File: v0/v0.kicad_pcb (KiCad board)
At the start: 2 copper layers, 101.5 x 83 mm, 35 parts, among them CON1 SNES-CONN, U1 SN74LV165APWR, U2 SN74LV165APWR, U3 SN74LV165APWR, U4 SN74LVC8T245PWR, U5 PIC12F629-ISN, U6 AMS1117-3.3

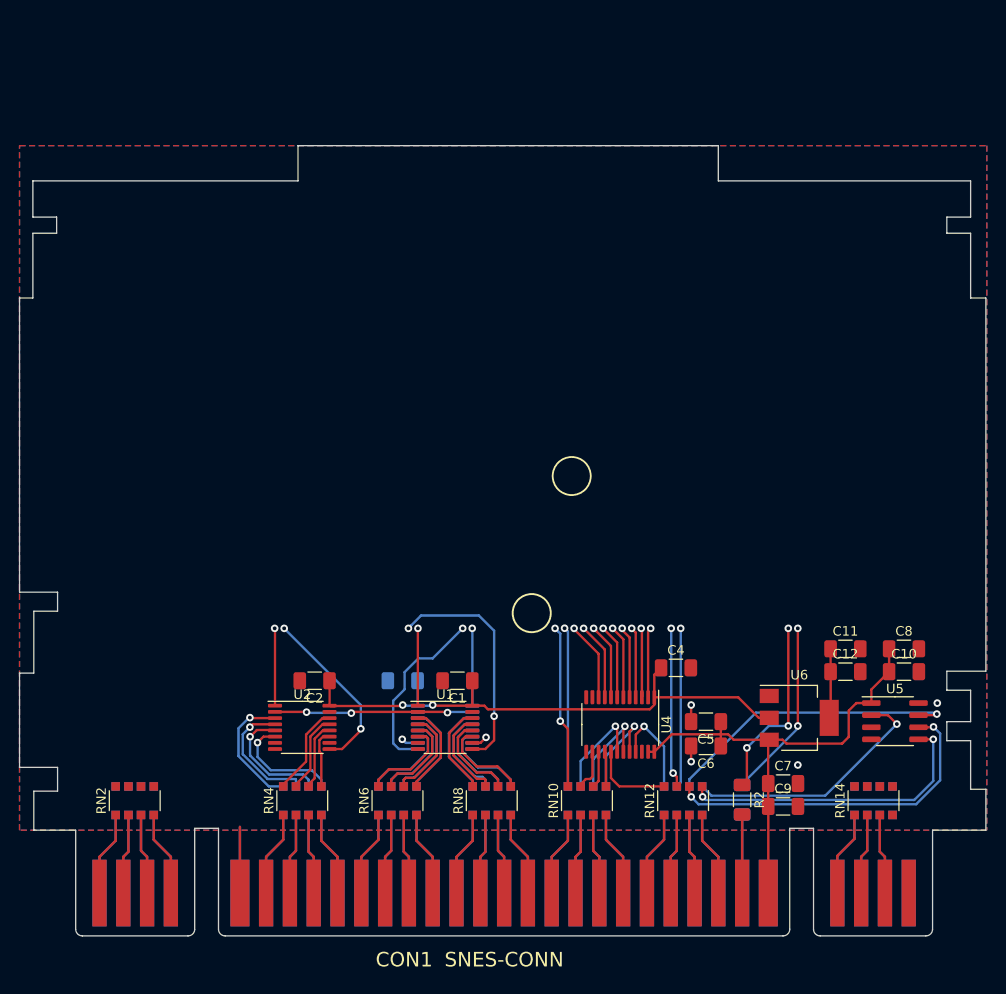
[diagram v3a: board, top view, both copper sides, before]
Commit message: Added RPi Pico footprint and routed traces to it
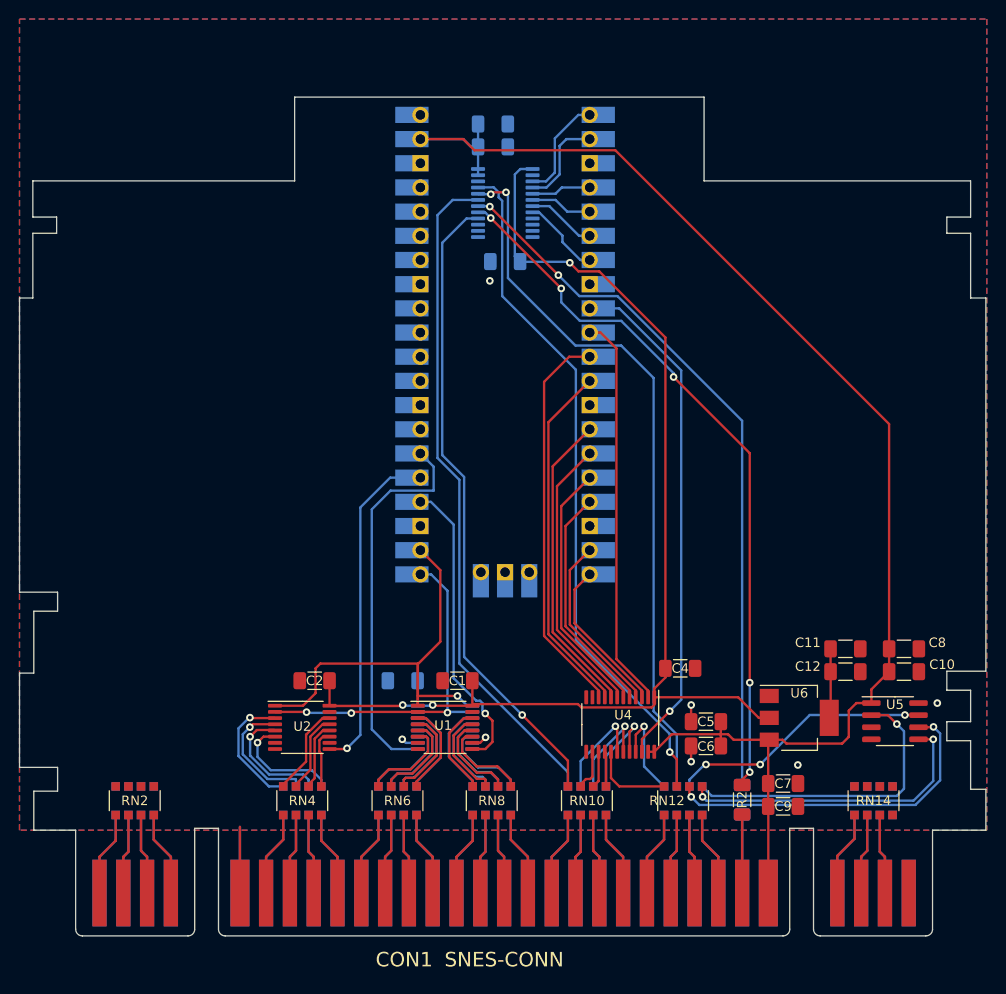
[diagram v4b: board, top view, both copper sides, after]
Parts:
- added C13: 0.1uF, Capacitor_SMD:C_1206_3216Metric_Pad1.33x1.80mm_HandSolder, B.Cu at (137.3, 63.0)
- added C14: 0.1uF, Capacitor_SMD:C_1206_3216Metric_Pad1.33x1.80mm_HandSolder, B.Cu at (136.0, 50.9)
- added C15: 1uF, Capacitor_SMD:C_1206_3216Metric_Pad1.33x1.80mm_HandSolder, B.Cu at (136.0, 48.5)
- added U7: SN74LVC8T245PWR, Package_SO:TSSOP-24_4.4x7.8mm_P0.65mm, B.Cu at (137.3, 56.8)
- added U8: Pico, RP-Pico:RPi_Pico_SMD_TH, B.Cu at (137.3, 71.7)
- moved C4 0.45 mm to (155.7, 105.7)
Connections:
- RN13 pad 5: unconnected-(RN13-Pad5) -> /YPA1
- RN13 pad 6: unconnected-(RN13-Pad6) -> /YPA3
- RN13 pad 7: unconnected-(RN13-Pad7) -> /YPA5
- U2 pad 1: /U2~{LD} -> /U1~{LD}
- U3 pad 1: /U3~{LD} -> /U1~{LD}
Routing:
- net +5V: track 53.2 -> 150.0 mm
- net +3.3V: track 66.9 -> 131.5 mm, vias 2 -> 3
- net /Y~{WR}: track 16.8 -> 75.7 mm, vias 1 -> 2
- net /YCPU_CLK: track 18.9 -> 75.3 mm
- net /Y~{RESET}: track 19.7 -> 76.0 mm, vias 3 -> 5
- net /Y~{RD}: track 16.8 -> 72.5 mm, vias 2 -> 1
- net /Y~{CE}: track 16.8 -> 70.6 mm, vias 1 -> 0
- net /D~{OE}: track 0.00 -> 52.5 mm, vias 0 -> 1
- net /Y~{IRQ}: track 17.2 -> 67.4 mm, vias 2 -> 1
- net /U1~{LD}: track 8.13 -> 46.6 mm
- net /DDIR: track 7.35 -> 41.5 mm, vias 1 -> 0
- net /D0: track 8.30 -> 41.4 mm, vias 1 -> 0
- net /D1: track 8.16 -> 37.5 mm, vias 1 -> 0
- net /D2: track 7.99 -> 32.3 mm, vias 1 -> 0
- net /D3: track 7.85 -> 29.7 mm, vias 1 -> 0
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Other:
- board size 101.5 x 83 mm -> 101.5 x 88.1 mm

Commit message: Connect /OE to GND; fix up minor routing
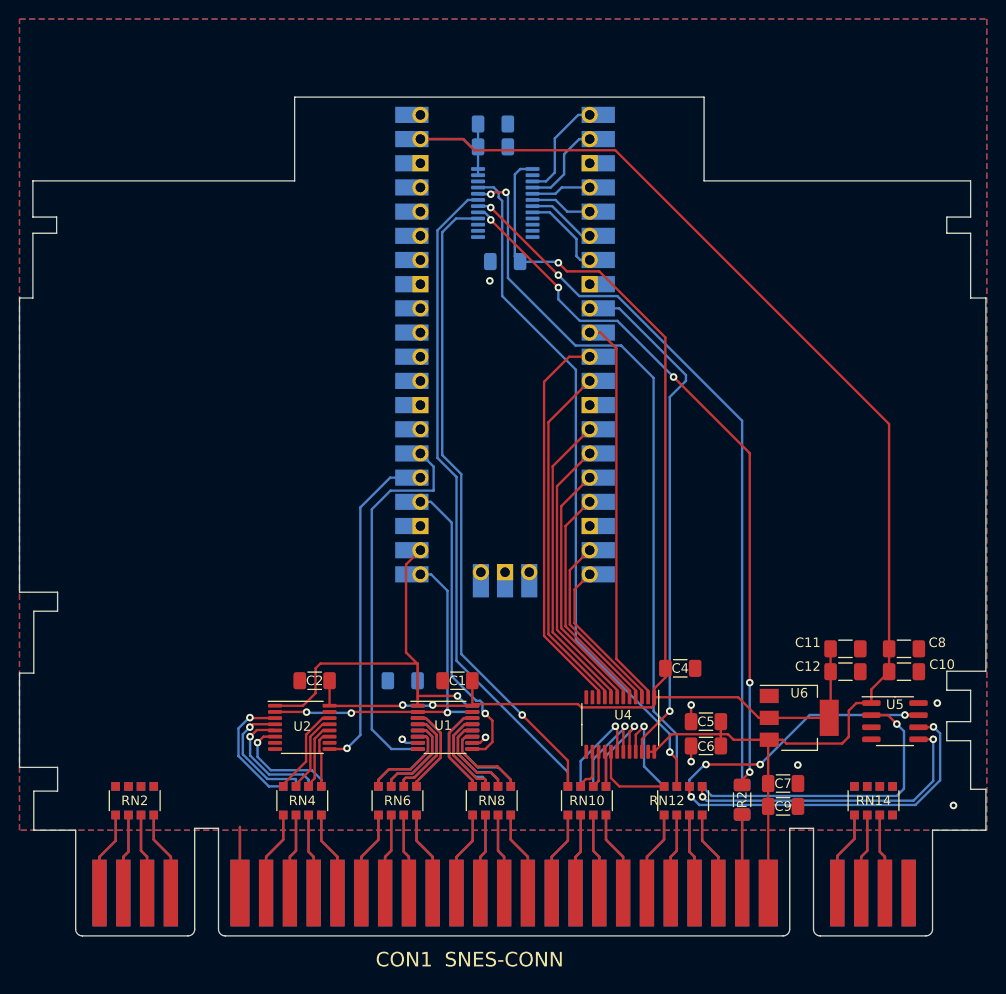
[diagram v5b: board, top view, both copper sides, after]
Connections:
- U7 pad 10: GND -> /U7A8
- U7 pad 14: GND -> /U7B8
- U7 pad 15: GND -> /U7B7
- U7 pad 22: unconnected-(U7-Pad22) -> GND
- U7 pad 9: GND -> /U7A7
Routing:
- net +3.3V: track 131.5 -> 137.8 mm
- net /Y~{RESET}: track 76.0 -> 75.0 mm
- net /Y~{CE}: track 70.6 -> 69.7 mm
- net /U1~{LD}: track 46.6 -> 45.9 mm
- net /~{IRQ}: track 8.47 -> 9.13 mm
- net /Y~{IRQ}: track 67.4 -> 68.0 mm
- net /~{WR}: track 9.87 -> 9.34 mm
- net GND: vias 7 -> 8

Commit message: Added front and back indicators; added title
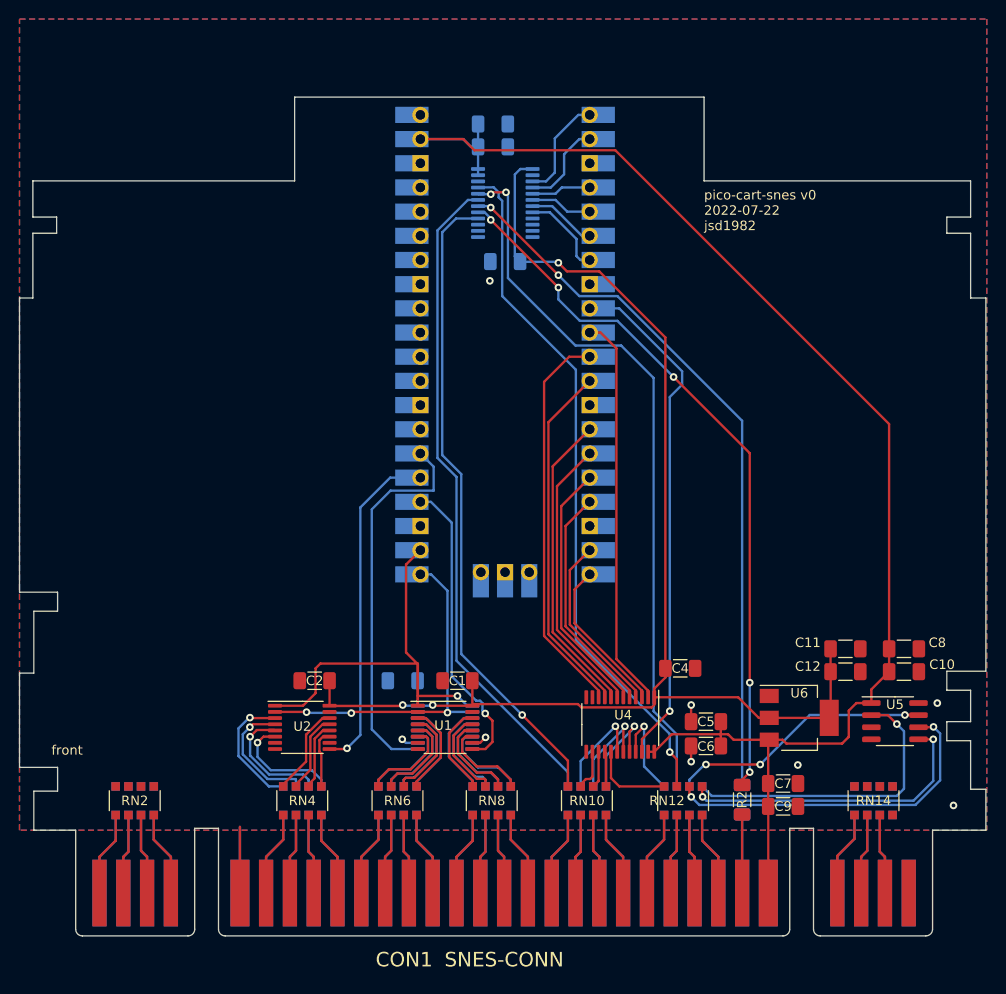
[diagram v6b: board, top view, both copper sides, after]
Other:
- board text added: "back"
- board text added: "front"
- board text added: "pico-cart-snes v0 2022-07-22 jsd1982"
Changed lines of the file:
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@@
     (property "Sheetname" "")
     (attr smd)
-    (fp_text reference "R1" (at 0 1.82 90) (layer "B.SilkS")
+    (fp_text reference "R1" (at 0 0.1 90) (layer "B.SilkS")
       (effects (font (size 1 1) (thickness 0.15)) (justify mirror))
     )
@@
       (rotate (xyz 0 0 0))
     )
+  )
+  (gr_text "back" (at 91.2 114.3) (layer "B.SilkS")
+    (effects (font (size 1 1) (thickness 0.15)) (justify mirror))
+  )
+  (gr_text "pico-cart-snes v0\n2022-07-22\njsd1982" (at 158.2 57.6) (layer "F.SilkS")
+    (effects (font (size 1 1) (thickness 0.15)) (justify left))
+  )
+  (gr_text "front" (at 91.3 114.3) (layer "F.SilkS")
+    (effects (font (size 1 1) (thickness 0.15)))
   )
   (segment (start 94.70072 125.49928) (end 96.4 123.8) (width 0.25) (layer "F.Cu") (net 1))
@@
   (segment (start 151.675 113.125) (end 154.599998 110.2) (width 0.25) (layer "F.Cu") (net 139))
   (via (at 154.599998 110.2) (size 0.8) (drill 0.4) (layers "F.Cu" "B.Cu") (net 139))
-  (segment (start 149.29 67.89) (end 156.3 74.9) (width 0.25) (layer "B.Cu") (net 139))
+  (segment (start 154.599998 77.200002) (end 154.599998 110.2) (width 0.25) (layer "B.Cu") (net 139))
+  (segment (start 155.9 75.9) (end 154.599998 77.200002) (width 0.25) (layer "B.Cu") (net 139))
+  (segment (start 155.9 74.5) (end 155.9 75.9) (width 0.25) (layer "B.Cu") (net 139))
+  (segment (start 149.29 67.89) (end 155.9 74.5) (width 0.25) (layer "B.Cu") (net 139))
   (segment (start 147.8 67.89) (end 149.29 67.89) (width 0.25) (layer "B.Cu") (net 139))
-  (segment (start 156.3 74.9) (end 156.3 75.5) (width 0.25) (layer "B.Cu") (net 139))
-  (segment (start 154.599998 77.200002) (end 154.599998 110.2) (width 0.25) (layer "B.Cu") (net 139))
-  (segment (start 156.3 75.5) (end 154.599998 77.200002) (width 0.25) (layer "B.Cu") (net 139))
   (segment (start 140.1875 57.8) (end 142 57.8) (width 0.25) (layer "B.Cu") (net 142))
   (segment (start 144.8 60.6) (end 144.8 62.4) (width 0.25) (layer "B.Cu") (net 142))

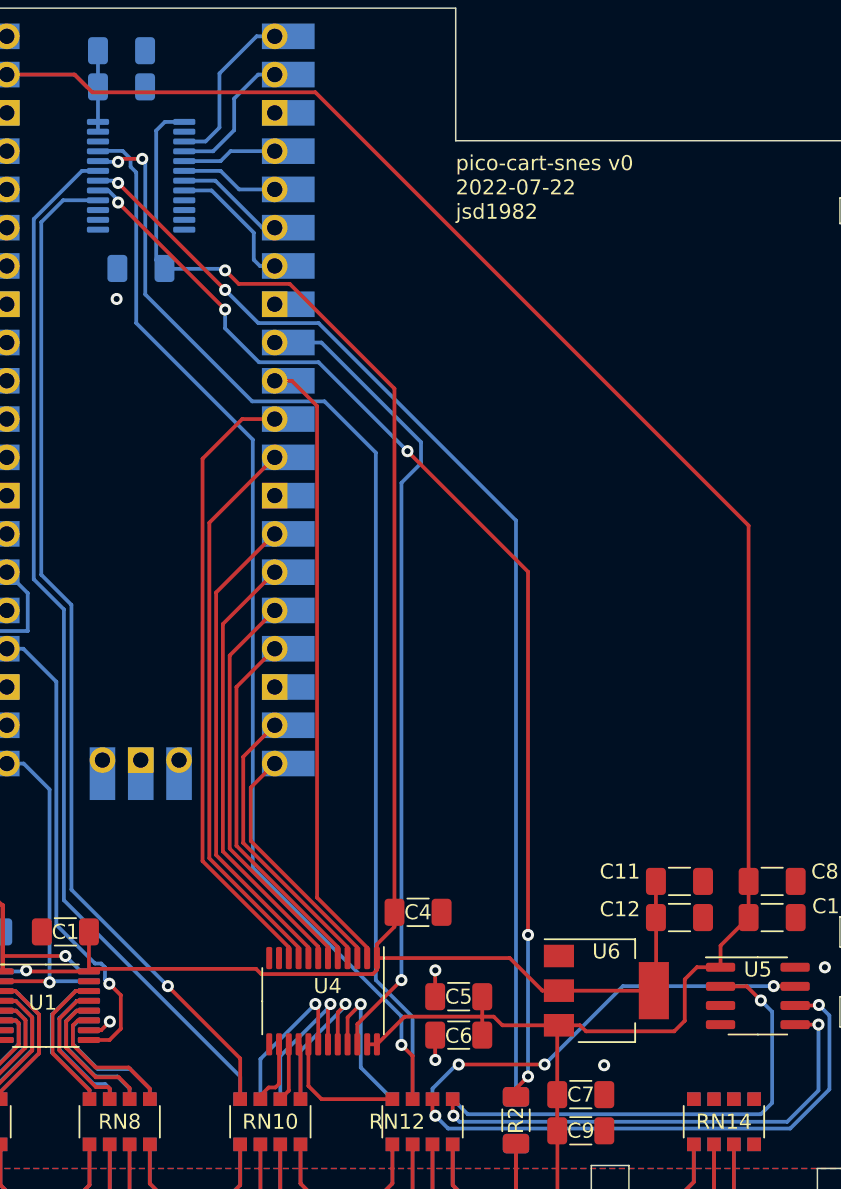
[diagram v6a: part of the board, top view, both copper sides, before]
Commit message: Add title to back layer; render front/back PCB and schematic
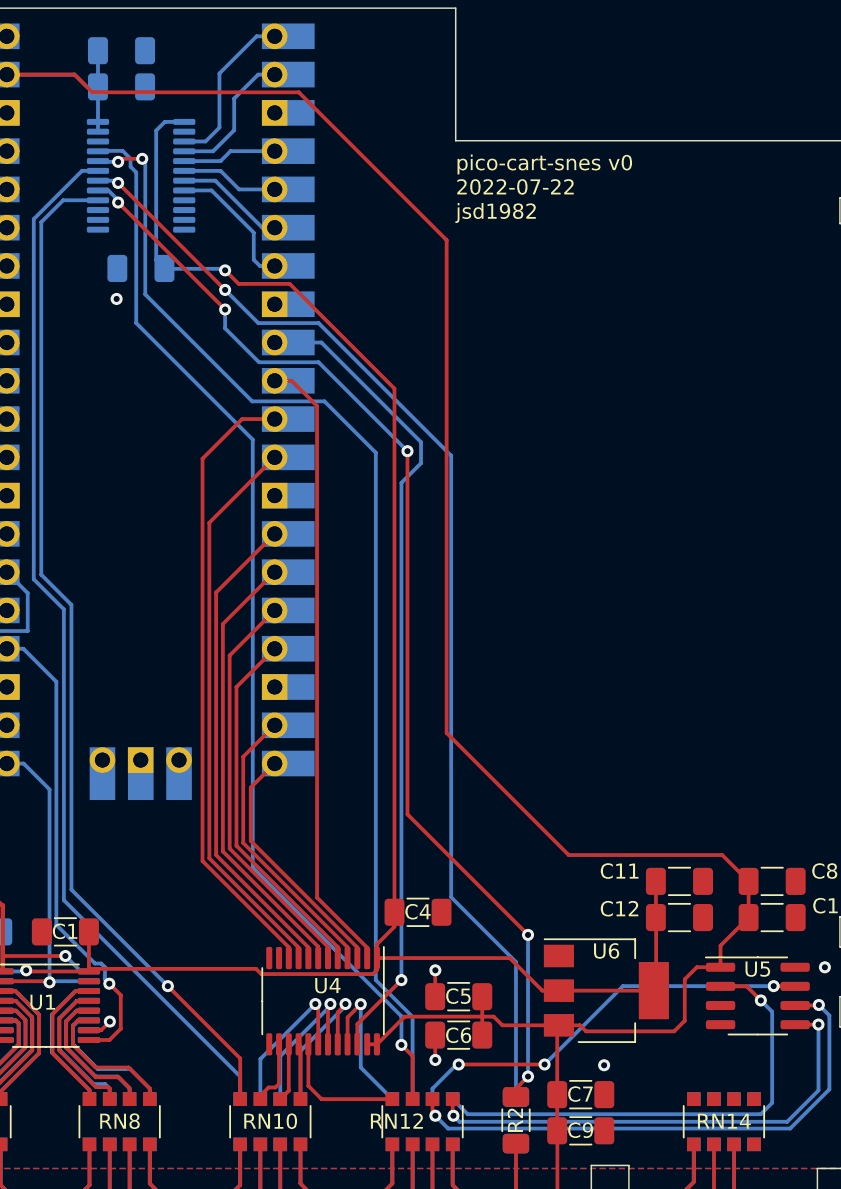
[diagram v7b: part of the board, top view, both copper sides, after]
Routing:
- net +5V: track 150.0 -> 155.3 mm
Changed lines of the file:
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@@
     )
+  )
+  (gr_text "pico-cart-snes v0\n2022-07-22\njsd1982" (at 172.8 57.6) (layer "B.SilkS")
+    (effects (font (size 1 1) (thickness 0.15)) (justify left mirror))
   )
   (gr_text "back" (at 91.2 114.3) (layer "B.SilkS")
@@
   (segment (start 162.20122 129.30038) (end 162.20122 121.05122) (width 0.25) (layer "F.Cu") (net 26))
   (segment (start 172.7 113.6) (end 173.4 112.9) (width 0.25) (layer "F.Cu") (net 27))
-  (segment (start 148.885 51.285) (end 177.6375 80.0375) (width 0.25) (layer "F.Cu") (net 27))
-  (segment (start 177.6375 80.0375) (end 177.6375 103.65) (width 0.25) (layer "F.Cu") (net 27))
+  (segment (start 134.085 51.285) (end 147.785 51.285) (width 0.25) (layer "F.Cu") (net 27))
   (segment (start 164.9375 117.8) (end 164.9375 113.3125) (width 0.25) (layer "F.Cu") (net 27))
   (segment (start 154.8125 112.625) (end 160.725 112.625) (width 0.25) (layer "F.Cu") (net 27))
@@
   (segment (start 164.9495 120.212) (end 164.9495 129.30038) (width 0.25) (layer "F.Cu") (net 27))
   (segment (start 165.05 113.2) (end 166.45 113.2) (width 0.25) (layer "F.Cu") (net 27))
-  (segment (start 134.085 51.285) (end 148.885 51.285) (width 0.25) (layer "F.Cu") (net 27))
+  (segment (start 157.6 61.1) (end 157.6 93.8) (width 0.25) (layer "F.Cu") (net 27))
   (segment (start 152.325 114.4625) (end 152.975 114.4625) (width 0.25) (layer "F.Cu") (net 27))
+  (segment (start 157.6 93.8) (end 165.7 101.9) (width 0.25) (layer "F.Cu") (net 27))
   (segment (start 174.205 109.345) (end 175.775 109.345) (width 0.25) (layer "F.Cu") (net 27))
   (segment (start 175.775 109.345) (end 175.775 107.9125) (width 0.25) (layer "F.Cu") (net 27))
+  (segment (start 128.41 50.11) (end 132.91 50.11) (width 0.25) (layer "F.Cu") (net 27))
   (segment (start 164.9375 117.8) (end 164.9375 120.2) (width 0.25) (layer "F.Cu") (net 27))
   (segment (start 161.3 113.2) (end 165.05 113.2) (width 0.25) (layer "F.Cu") (net 27))
@@
   (segment (start 173.4 110.15) (end 174.205 109.345) (width 0.25) (layer "F.Cu") (net 27))
   (segment (start 177.6375 106.05) (end 177.6375 103.65) (width 0.25) (layer "F.Cu") (net 27))
+  (segment (start 159.9625 111.3) (end 159.9625 112.6375) (width 0.25) (layer "F.Cu") (net 27))
+  (segment (start 165.7 101.9) (end 175.8875 101.9) (width 0.25) (layer "F.Cu") (net 27))
+  (segment (start 160.725 112.625) (end 161.3 113.2) (width 0.25) (layer "F.Cu") (net 27))
+  (segment (start 175.8875 101.9) (end 177.6375 103.65) (width 0.25) (layer "F.Cu") (net 27))
+  (segment (start 159.9625 113.85) (end 159.9625 112.6375) (width 0.25) (layer "F.Cu") (net 27))
   (segment (start 132.91 50.11) (end 134.085 51.285) (width 0.25) (layer "F.Cu") (net 27))
-  (segment (start 159.9625 111.3) (end 159.9625 112.6375) (width 0.25) (layer "F.Cu") (net 27))
-  (segment (start 160.725 112.625) (end 161.3 113.2) (width 0.25) (layer "F.Cu") (net 27))
-  (segment (start 159.9625 113.85) (end 159.9625 112.6375) (width 0.25) (layer "F.Cu") (net 27))
   (segment (start 173.4 112.9) (end 173.4 110.15) (width 0.25) (layer "F.Cu") (net 27))
-  (segment (start 128.41 50.11) (end 132.91 50.11) (width 0.25) (layer "F.Cu") (net 27))
+  (segment (start 147.785 51.285) (end 157.6 61.1) (width 0.25) (layer "F.Cu") (net 27))
   (segment (start 134.4625 50.925) (end 133.725 50.925) (width 0.25) (layer "B.Cu") (net 27))
   (segment (start 134.4625 50.925) (end 134.4625 53.25) (width 0.25) (layer "B.Cu") (net 27))
@@
   (via (at 142.9 64.4) (size 0.8) (drill 0.4) (layers "F.Cu" "B.Cu") (net 109))
   (segment (start 134.4625 57.15) (end 135.65 57.15) (width 0.25) (layer "B.Cu") (net 109))
+  (segment (start 162.2 117.95) (end 162.2 109) (width 0.25) (layer "B.Cu") (net 109))
+  (segment (start 135.65 57.15) (end 135.8 57.3) (width 0.25) (layer "B.Cu") (net 109))
+  (segment (start 157.9 75.4) (end 149.1 66.6) (width 0.25) (layer "B.Cu") (net 109))
+  (segment (start 145.1 66.6) (end 142.9 64.4) (width 0.25) (layer "B.Cu") (net 109))
+  (segment (start 162.2 109) (end 157.9 104.7) (width 0.25) (layer "B.Cu") (net 109))
   (segment (start 149.1 66.6) (end 145.1 66.6) (width 0.25) (layer "B.Cu") (net 109))
-  (segment (start 135.65 57.15) (end 135.8 57.3) (width 0.25) (layer "B.Cu") (net 109))
-  (segment (start 162.2 79.7) (end 149.1 66.6) (width 0.25) (layer "B.Cu") (net 109))
-  (segment (start 162.2 117.95) (end 162.2 79.7) (width 0.25) (layer "B.Cu") (net 109))
-  (segment (start 145.1 66.6) (end 142.9 64.4) (width 0.25) (layer "B.Cu") (net 109))
+  (segment (start 157.9 104.7) (end 157.9 75.4) (width 0.25) (layer "B.Cu") (net 109))
   (segment (start 162.2 117.95) (end 162.2 117.4) (width 0.25) (layer "F.Cu") (net 110))
-  (segment (start 163 83.1) (end 163 107.2) (width 0.25) (layer "F.Cu") (net 110))
   (segment (start 162.2 117.4) (end 163 116.6) (width 0.25) (layer "F.Cu") (net 110))
+  (segment (start 155 99.2) (end 163 107.2) (width 0.25) (layer "F.Cu") (net 110))
   (segment (start 142.9 65.7) (end 135.8 58.6) (width 0.25) (layer "F.Cu") (net 110))
-  (segment (start 155 75.1) (end 163 83.1) (width 0.25) (layer "F.Cu") (net 110))
+  (segment (start 155 75.1) (end 155 99.2) (width 0.25) (layer "F.Cu") (net 110))
   (via (at 163 116.6) (size 0.8) (drill 0.4) (layers "F.Cu" "B.Cu") (net 110))
   (via (at 155 75.1) (size 0.8) (drill 0.4) (layers "F.Cu" "B.Cu") (net 110))
